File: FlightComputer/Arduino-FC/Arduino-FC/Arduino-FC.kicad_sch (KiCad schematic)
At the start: 30 parts, among them J1 Conn_01x04, J2 Conn_01x08, J3 Conn_01x06, J4 Conn_01x03, J5 Screw_Terminal_01x02, J6 Conn_01x02, J7 Conn_01x02, U1 NRF24L01_Breakout

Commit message: Major Layout + Logo
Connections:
- net +5V: now also A1.2 (IOREF), C4.1, C5.1, R3.1, VR1.3 (VOUT)
- no-connect marks 23 -> 22
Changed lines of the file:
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@@
 	(title_block
 		(title "Arduino Flight Computer")
-		(date "2026-04-30")
+		(date "2026-05-26")
 		(rev "v1.0")
 		(company "Team 'Lite Work: CANSAT STEC Initiative")
@@
 	)
 	(junction
+		(at 176.53 26.67)
+		(diameter 0)
+		(color 0 0 0 0)
+	)
+	(junction
 		(at 138.43 129.54)
 		(diameter 0)
@@
 	)
 	(junction
-		(at 148.59 74.93)
-		(diameter 0)
-		(color 0 0 0 0)
-	)
-	(junction
 		(at 82.55 50.8)
 		(diameter 0)
@@
 		(color 0 0 0 0)
 	)
+	(junction
+		(at 153.67 74.93)
+		(diameter 0)
+		(color 0 0 0 0)
+	)
 	(no_connect
 		(at 227.33 104.14)
@@
 	)
 	(no_connect
-		(at 151.13 90.17)
-	)
-	(no_connect
 		(at 125.73 110.49)
 	)
@@
 	(wire
 		(pts
+			(xy 153.67 74.93) (xy 154.94 74.93)
+		)
+		(stroke
+			(width 0)
+			(type default)
+		)
+	)
+	(wire
+		(pts
 			(xy 170.18 46.99) (xy 170.18 49.53)
 		)
@@
 	(wire
 		(pts
-			(xy 143.51 74.93) (xy 148.59 74.93)
+			(xy 143.51 74.93) (xy 153.67 74.93)
 		)
 		(stroke
@@
 	(wire
 		(pts
-			(xy 148.59 74.93) (xy 154.94 74.93)
-		)
-		(stroke
-			(width 0)
-			(type default)
-		)
-	)
-	(wire
-		(pts
 			(xy 66.04 38.1) (xy 71.12 38.1)
 		)
@@
 	(wire
 		(pts
+			(xy 176.53 22.86) (xy 176.53 26.67)
+		)
+		(stroke
+			(width 0)
+			(type default)
+		)
+	)
+	(wire
+		(pts
 			(xy 217.17 46.99) (xy 227.33 46.99)
 		)
@@
 	(wire
 		(pts
+			(xy 151.13 90.17) (xy 153.67 90.17)
+		)
+		(stroke
+			(width 0)
+			(type default)
+		)
+	)
+	(wire
+		(pts
 			(xy 71.12 26.67) (xy 71.12 29.21)
 		)
@@
 	(wire
 		(pts
+			(xy 153.67 90.17) (xy 153.67 74.93)
+		)
+		(stroke
+			(width 0)
+			(type default)
+		)
+	)
+	(wire
+		(pts
 			(xy 217.17 54.61) (xy 227.33 54.61)
 		)
@@
 	(wire
 		(pts
-			(xy 148.59 74.93) (xy 148.59 71.12)
+			(xy 153.67 74.93) (xy 153.67 71.12)
 		)
 		(stroke
@@
 	(symbol
 		(lib_id "power:+5V")
-		(at 148.59 71.12 0)
+		(at 153.67 71.12 0)
 		(unit 1)
 		(exclude_from_sim no)
@@
 		(fields_autoplaced yes)
 		(property "Reference" "#PWR011"
-			(at 148.59 74.93 0)
+			(at 153.67 74.93 0)
 			(effects
 				(font
@@
 		)
 		(property "Value" "+5V"
-			(at 148.59 66.04 0)
+			(at 153.67 66.04 0)
 			(effects
 				(font
@@
 		)
 		(property "Footprint" ""
-			(at 148.59 71.12 0)
+			(at 153.67 71.12 0)
 			(effects
 				(font
@@
 		)
 		(property "Datasheet" ""
-			(at 148.59 71.12 0)
+			(at 153.67 71.12 0)
 			(effects
 				(font
@@
 		)
 		(property "Description" "Power symbol creates a global label with name \"+5V\""
-			(at 148.59 71.12 0)
+			(at 153.67 71.12 0)
 			(effects
 				(font
@@
 					(unit 1)
 				)
+			)
+		)
+	)
+	(symbol
+		(lib_id "power:+5V")
+		(at 176.53 22.86 0)
+		(unit 1)
+		(exclude_from_sim no)
+		(in_bom yes)
+		(on_board yes)
+		(dnp no)
+		(fields_autoplaced yes)
+		(property "Reference" "#PWR022"
+			(at 176.53 26.67 0)
+			(effects
+				(font
+					(size 1.27 1.27)
+				)
+				(hide yes)
+			)
+		)
+		(property "Value" "+5V"
+			(at 176.53 17.78 0)
+			(effects
+				(font
+					(size 1.27 1.27)
+				)
+			)
+		)
+		(property "Footprint" ""
+			(at 176.53 22.86 0)
+			(effects
+				(font
+					(size 1.27 1.27)
+				)
+				(hide yes)
+			)
+		)
+		(property "Datasheet" ""
+			(at 176.53 22.86 0)
+			(effects
+				(font
+					(size 1.27 1.27)
+				)
+				(hide yes)
+			)
+		)
+		(property "Description" "Power symbol creates a global label with name \"+5V\""
+			(at 176.53 22.86 0)
+			(effects
+				(font
+					(size 1.27 1.27)
+				)
+				(hide yes)
+			)
+		)
+		(pin "1"
+		)
+		(instances
+			(project "Arduino-FC"
+				(path "/979d3eec-a24a-4073-bdb5-1e3cad04034a"
+					(reference "#PWR022")
+					(unit 1)
+				)

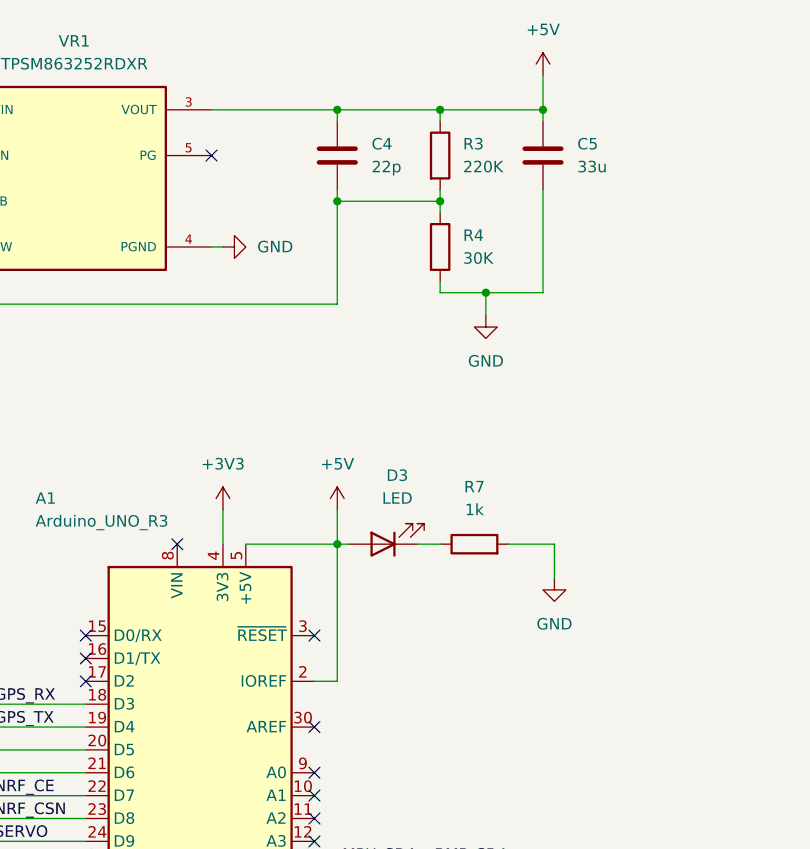
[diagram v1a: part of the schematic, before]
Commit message: Revert "Major Layout + Logo"
This reverts commit 6804596b28cb7cea65c62195238a1a9f434acbb5.
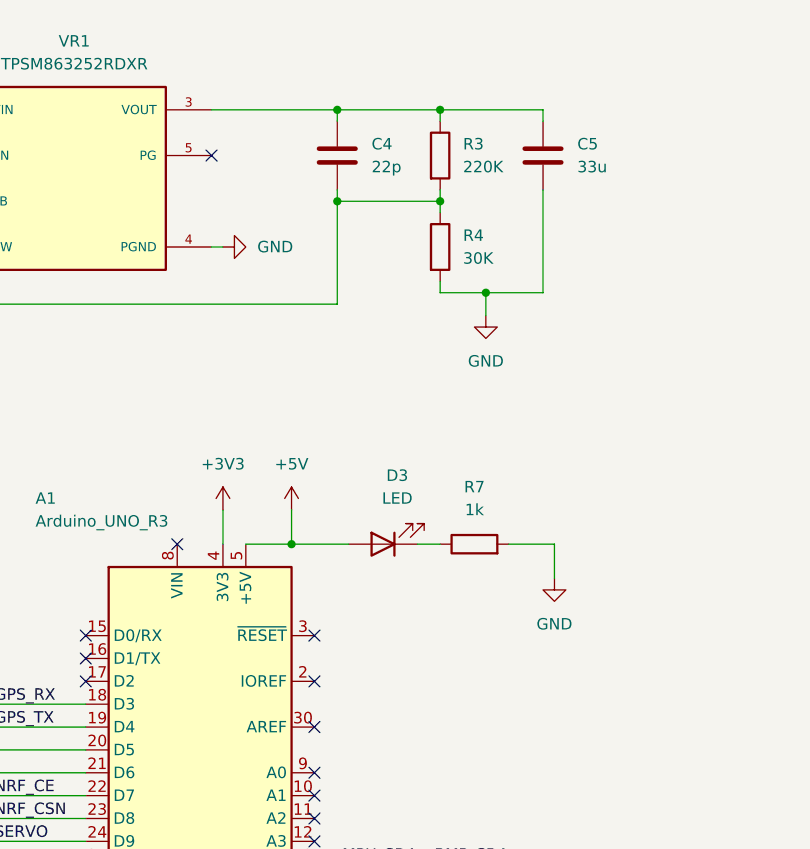
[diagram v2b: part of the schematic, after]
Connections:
- net +5V: no longer A1.2 (IOREF), C4.1, C5.1, R3.1, VR1.3 (VOUT)
- new net: C4.1, C5.1, R3.1, VR1.3 (VOUT)
- no-connect marks 22 -> 23
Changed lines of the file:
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@@
 	(title_block
 		(title "Arduino Flight Computer")
-		(date "2026-05-26")
+		(date "2026-04-30")
 		(rev "v1.0")
 		(company "Team 'Lite Work: CANSAT STEC Initiative")
@@
 	)
 	(junction
-		(at 176.53 26.67)
-		(diameter 0)
-		(color 0 0 0 0)
-	)
-	(junction
 		(at 138.43 129.54)
 		(diameter 0)
@@
 	)
 	(junction
+		(at 148.59 74.93)
+		(diameter 0)
+		(color 0 0 0 0)
+	)
+	(junction
 		(at 82.55 50.8)
 		(diameter 0)
@@
 		(color 0 0 0 0)
 	)
-	(junction
-		(at 153.67 74.93)
-		(diameter 0)
-		(color 0 0 0 0)
-	)
 	(no_connect
 		(at 227.33 104.14)
@@
 	)
 	(no_connect
+		(at 151.13 90.17)
+	)
+	(no_connect
 		(at 125.73 110.49)
 	)
@@
 	(wire
 		(pts
-			(xy 153.67 74.93) (xy 154.94 74.93)
-		)
-		(stroke
-			(width 0)
-			(type default)
-		)
-	)
-	(wire
-		(pts
 			(xy 170.18 46.99) (xy 170.18 49.53)
 		)
@@
 	(wire
 		(pts
-			(xy 143.51 74.93) (xy 153.67 74.93)
+			(xy 143.51 74.93) (xy 148.59 74.93)
 		)
 		(stroke
@@
 	(wire
 		(pts
+			(xy 148.59 74.93) (xy 154.94 74.93)
+		)
+		(stroke
+			(width 0)
+			(type default)
+		)
+	)
+	(wire
+		(pts
 			(xy 66.04 38.1) (xy 71.12 38.1)
 		)
@@
 	(wire
 		(pts
-			(xy 176.53 22.86) (xy 176.53 26.67)
-		)
-		(stroke
-			(width 0)
-			(type default)
-		)
-	)
-	(wire
-		(pts
 			(xy 217.17 46.99) (xy 227.33 46.99)
 		)
@@
 	(wire
 		(pts
-			(xy 151.13 90.17) (xy 153.67 90.17)
-		)
-		(stroke
-			(width 0)
-			(type default)
-		)
-	)
-	(wire
-		(pts
 			(xy 71.12 26.67) (xy 71.12 29.21)
 		)
@@
 	(wire
 		(pts
-			(xy 153.67 90.17) (xy 153.67 74.93)
-		)
-		(stroke
-			(width 0)
-			(type default)
-		)
-	)
-	(wire
-		(pts
 			(xy 217.17 54.61) (xy 227.33 54.61)
 		)
@@
 	(wire
 		(pts
-			(xy 153.67 74.93) (xy 153.67 71.12)
+			(xy 148.59 74.93) (xy 148.59 71.12)
 		)
 		(stroke
@@
 	(symbol
 		(lib_id "power:+5V")
-		(at 153.67 71.12 0)
+		(at 148.59 71.12 0)
 		(unit 1)
 		(exclude_from_sim no)
@@
 		(fields_autoplaced yes)
 		(property "Reference" "#PWR011"
-			(at 153.67 74.93 0)
+			(at 148.59 74.93 0)
 			(effects
 				(font
@@
 		)
 		(property "Value" "+5V"
-			(at 153.67 66.04 0)
+			(at 148.59 66.04 0)
 			(effects
 				(font
@@
 		)
 		(property "Footprint" ""
-			(at 153.67 71.12 0)
+			(at 148.59 71.12 0)
 			(effects
 				(font
@@
 		)
 		(property "Datasheet" ""
-			(at 153.67 71.12 0)
+			(at 148.59 71.12 0)
 			(effects
 				(font
@@
 		)
 		(property "Description" "Power symbol creates a global label with name \"+5V\""
-			(at 153.67 71.12 0)
+			(at 148.59 71.12 0)
 			(effects
 				(font
@@
 					(unit 1)
 				)
-			)
-		)
-	)
-	(symbol
-		(lib_id "power:+5V")
-		(at 176.53 22.86 0)
-		(unit 1)
-		(exclude_from_sim no)
-		(in_bom yes)
-		(on_board yes)
-		(dnp no)
-		(fields_autoplaced yes)
-		(property "Reference" "#PWR022"
-			(at 176.53 26.67 0)
-			(effects
-				(font
-					(size 1.27 1.27)
-				)
-				(hide yes)
-			)
-		)
-		(property "Value" "+5V"
-			(at 176.53 17.78 0)
-			(effects
-				(font
-					(size 1.27 1.27)
-				)
-			)
-		)
-		(property "Footprint" ""
-			(at 176.53 22.86 0)
-			(effects
-				(font
-					(size 1.27 1.27)
-				)
-				(hide yes)
-			)
-		)
-		(property "Datasheet" ""
-			(at 176.53 22.86 0)
-			(effects
-				(font
-					(size 1.27 1.27)
-				)
-				(hide yes)
-			)
-		)
-		(property "Description" "Power symbol creates a global label with name \"+5V\""
-			(at 176.53 22.86 0)
-			(effects
-				(font
-					(size 1.27 1.27)
-				)
-				(hide yes)
-			)
-		)
-		(pin "1"
-		)
-		(instances
-			(project "Arduino-FC"
-				(path "/979d3eec-a24a-4073-bdb5-1e3cad04034a"
-					(reference "#PWR022")
-					(unit 1)
-				)
